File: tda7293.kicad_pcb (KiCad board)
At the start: 2 copper layers, 100 x 48 mm, 70 parts, among them J1 Screw_Terminal_01x04, J2 Screw_Terminal_01x04, J3 Screw_Terminal_01x02, J4 Screw_Terminal_01x03, Q1 BSS84, Q2 2N7002, U1 TDA7293, U2 TDA7293, U3 PC817, U4 MCP1792

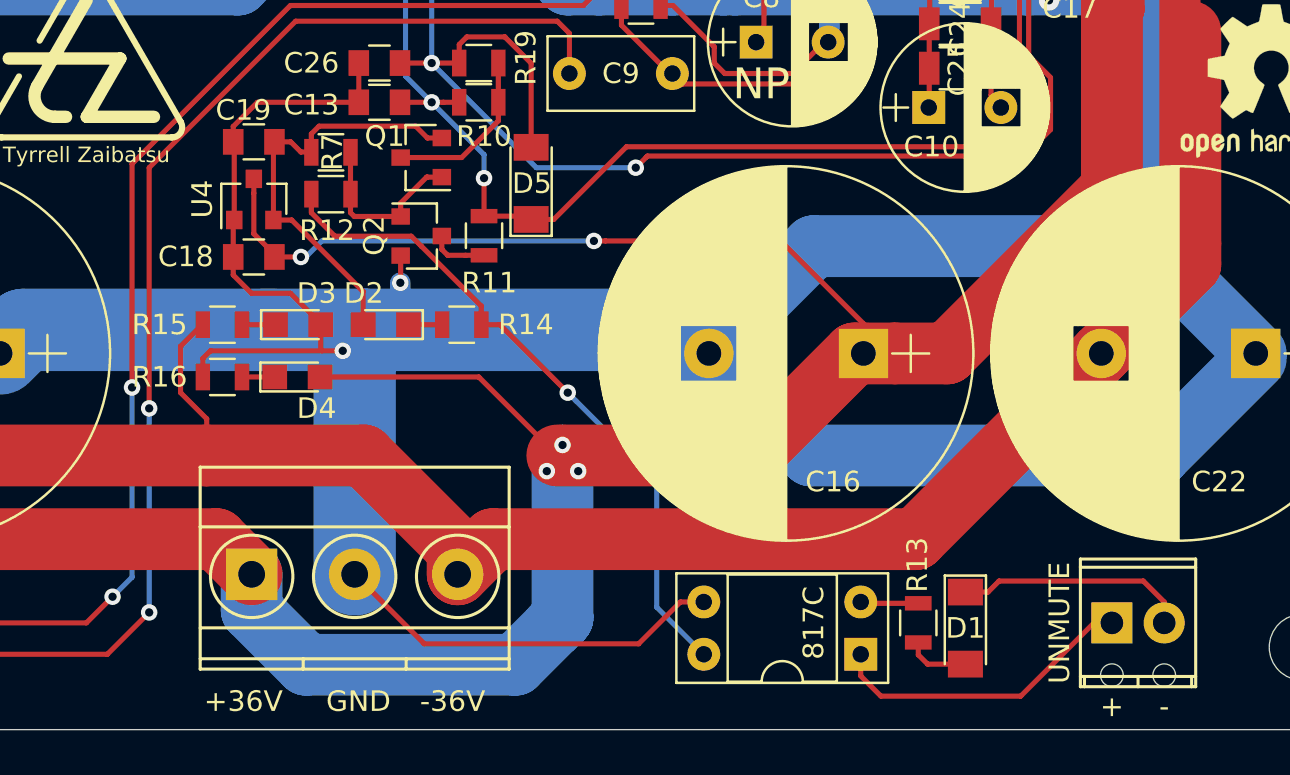
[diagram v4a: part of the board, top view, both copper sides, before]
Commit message: moved a resistor, plotted ready for manufacture
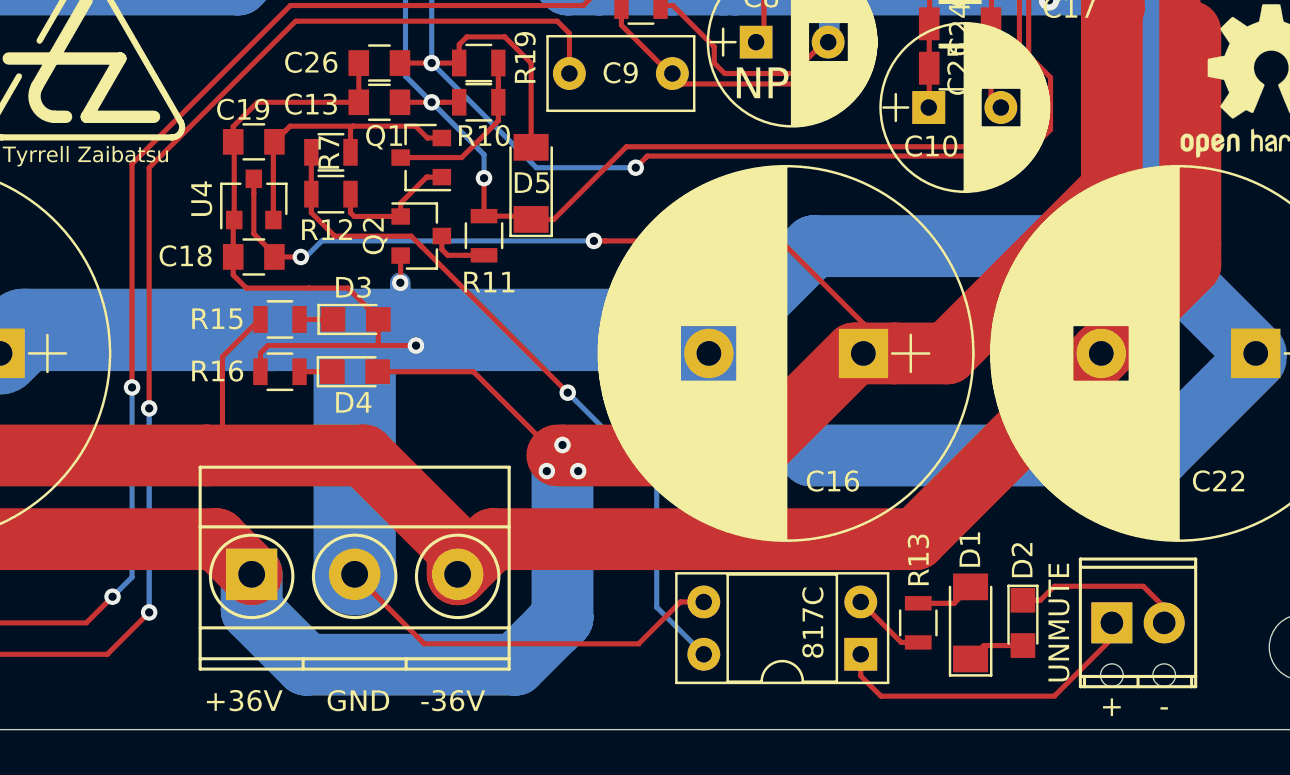
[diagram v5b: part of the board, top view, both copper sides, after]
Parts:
- removed R14: 1k, Resistors_SMD:R_0805
- moved D2 34.2 mm to (107.4, 67.8), turned to 270 degrees
- moved D3 2.81 mm to (75.0, 53.1)
- moved D4 2.81 mm to (75.0, 55.6)
- moved R15 2.81 mm to (71.4, 53.1)
- moved R16 2.81 mm to (71.4, 55.6)
- moved D1 0.36 mm to (104.9, 67.8), turned to 90 degrees
- turned R13 to 270 degrees
- turned R7 to 0 degrees
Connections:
- D2 pad 2: /5V -> Net-(D1-Pad1)
- J3 pad 2: Net-(D1-Pad1) -> Net-(D2-Pad1)
- R7 pad 1: Net-(Q1-Pad1) -> Net-(R12-Pad1)
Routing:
- net Net-(D1-Pad1): track 11.7 -> 2.81 mm
- net /5V: track 20.9 -> 13.9 mm
- net Net-(D2-Pad1): track 1.45 -> 8.32 mm
- net /GND: track 511.8 -> 515.3 mm
- net /VCC: track 212.3 -> 209.6 mm
- net Net-(Q1-Pad1): track 8.61 -> 6.58 mm
- net Net-(R12-Pad1): track 33.4 -> 34.5 mm
- net Net-(R13-Pad2): track 2.82 -> 3.70 mm

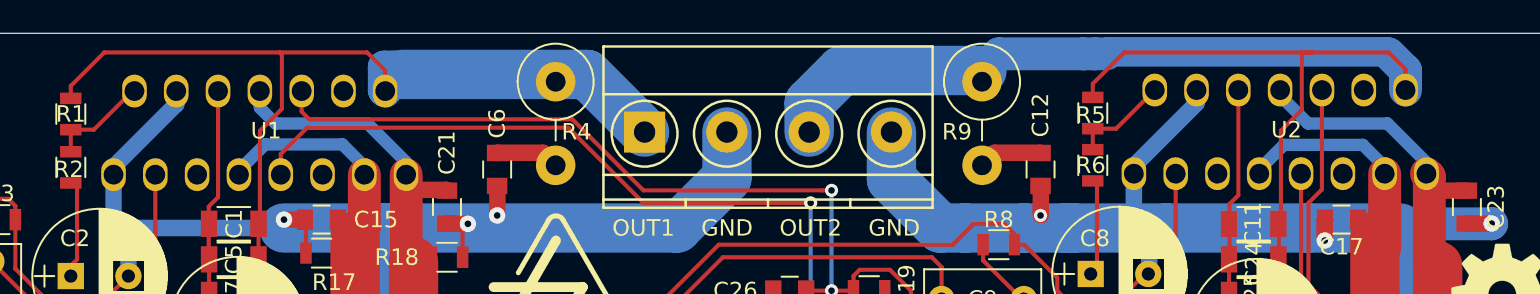
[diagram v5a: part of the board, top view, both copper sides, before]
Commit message: fixed footprint - matching hole size
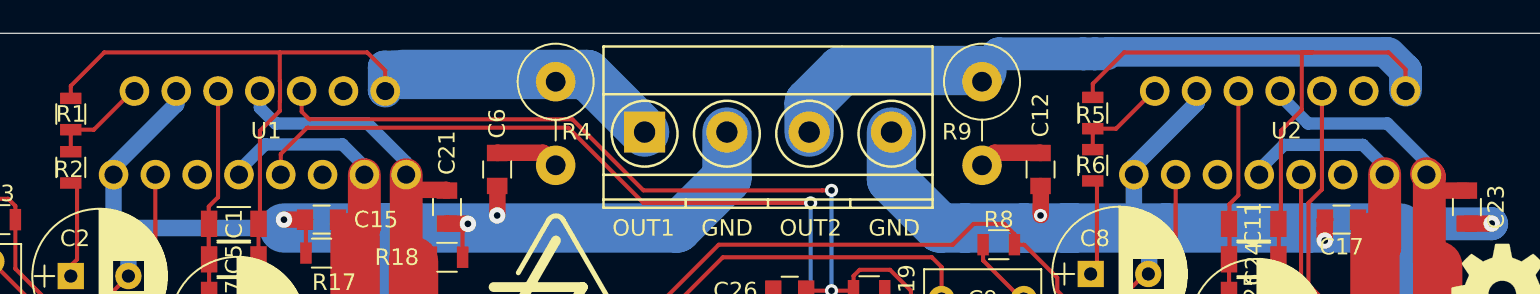
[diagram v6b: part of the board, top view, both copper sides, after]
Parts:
- moved U2 0.06 mm to (106.0, 28.5)
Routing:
- net Net-(C3-Pad1): track 22.8 -> 22.3 mm

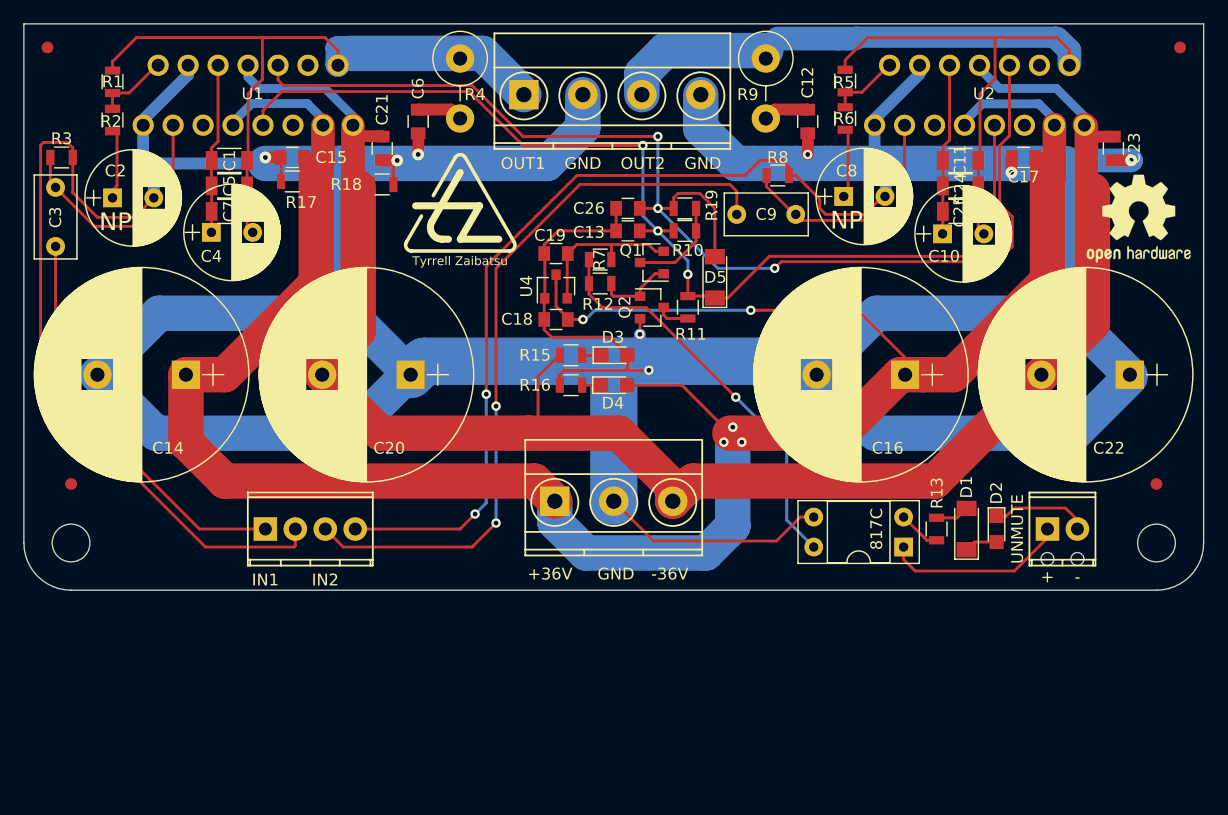
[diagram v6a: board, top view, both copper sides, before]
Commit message: Redrafted as Rev.B: hum-break resistors, better GND topology, fuses, room for heatsink screwdrivers!
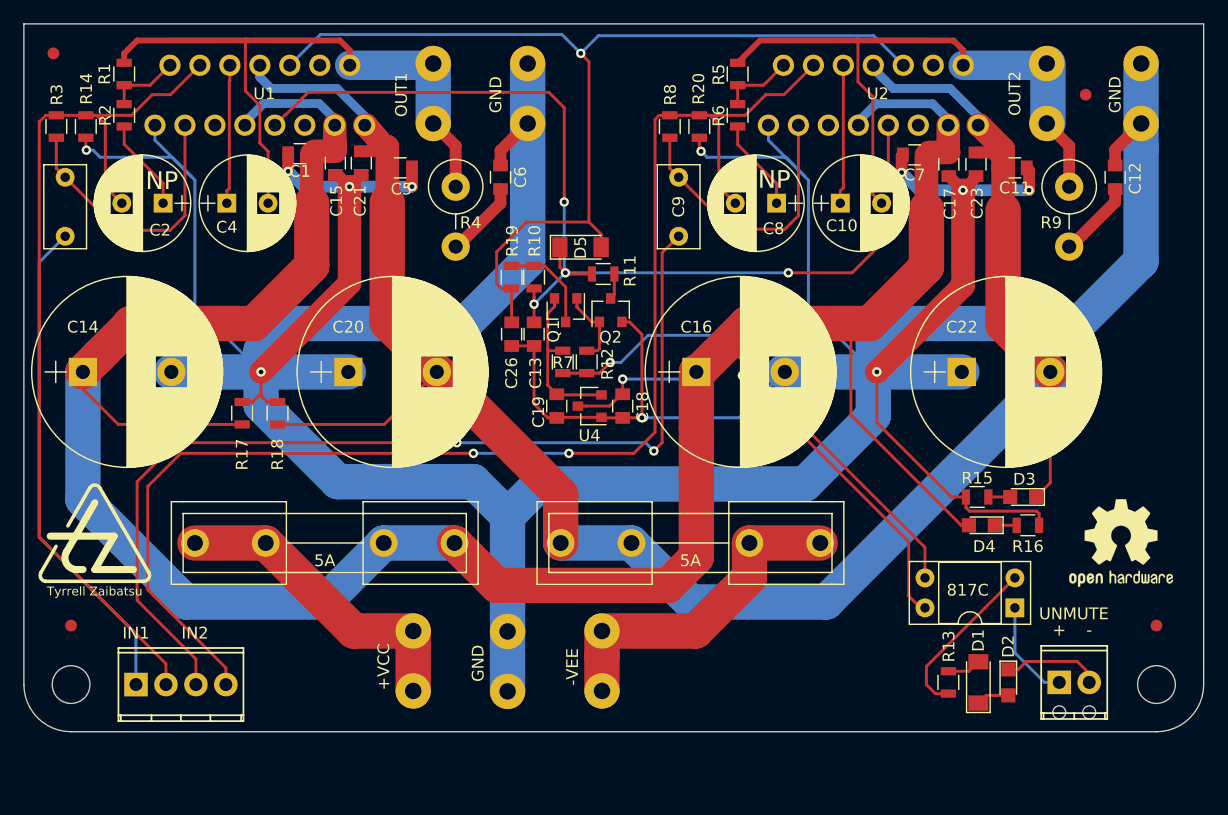
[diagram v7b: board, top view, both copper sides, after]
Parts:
- removed C24, C25: 10u, Capacitors_SMD:C_1206
- added F1: 4A, power:Fuseholder5x20_6mm, F.Cu at (60.5, 69.0)
- added F2: 4A, power:Fuseholder5x20_6mm, F.Cu at (71.5, 69.0)
- added J5: Conn_01x01_Male, power:FASTON250P_5.08mm_male_vertical, F.Cu at (111.7, 30.9)
- added J6: Conn_01x01_Male, power:FASTON250P_5.08mm_male_vertical, F.Cu at (119.7, 30.9)
- added J7: Conn_01x01_Male, power:FASTON250P_5.08mm_male_vertical, F.Cu at (58.0, 79.0)
- added J8: Conn_01x01_Male, power:FASTON250P_5.08mm_male_vertical, F.Cu at (66.0, 79.0)
- added J9: Conn_01x01_Male, power:FASTON250P_5.08mm_male_vertical, F.Cu at (74.0, 79.0)
- added R14: 15, Resistors_SMD:R_0805, F.Cu at (30.2, 33.7)
- added R20: 15, Resistors_SMD:R_0805, F.Cu at (82.2, 33.7)
- C1, C11, C5, C7: value 10u -> 1u; footprint Capacitors_SMD:C_1206 -> Capacitors_SMD:C_0805
- C14, C16, C20, C22: value 3300u -> 1000u; footprint Capacitors_ThroughHole:CP_Radial_D18.0mm_P7.50mm -> Capacitors_ThroughHole:CP_Radial_D16.0mm_P7.50mm
- J2: value Screw_Terminal_01x04 -> Conn_01x01_Male; footprint Terminals_Phoenix:TerminalBlock_Phoenix_MKDS1.5-4pol -> power:FASTON250P_5.08mm_male_vertical
- J4: value Screw_Terminal_01x03 -> Conn_01x01_Male; footprint Terminals_Phoenix:TerminalBlock_Phoenix_MKDS1.5-3pol -> power:FASTON250P_5.08mm_male_vertical
- moved FID3 95.5 mm to (27.5, 27.5)
- moved FID2 88.1 mm to (115.0, 31.0)
- moved C7 58.3 mm to (100.5, 36.1)
- moved REF** 41.8 mm to (31.0, 69.0)
- moved R16 40.5 mm to (110.1, 67.5), turned to 0 degrees
- moved D3 36.7 mm to (109.7, 65.1), turned to 180 degrees
- moved R15 36.5 mm to (105.8, 65.1), turned to 0 degrees
- moved J4 34.6 mm to (67.7, 30.9)
- moved D4 33.4 mm to (106.2, 67.5), turned to 180 degrees
- moved R9 27.9 mm to (113.6, 38.8)
- moved REF*** 27.5 mm to (118.0, 69.0)
- moved C12 26.5 mm to (117.5, 38.0), turned to 90 degrees
- moved R18 21.3 mm to (46.5, 58.0), turned to 90 degrees
- moved R17 20.1 mm to (43.5, 58.0), turned to 270 degrees
- moved C16 17.7 mm to (82.0, 54.5), turned to 0 degrees
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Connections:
- C1 pad 1: /OUT1 -> /VCC
- C1 pad 2: Net-(C1-Pad2) -> /GND
- C11 pad 1: /OUT2 -> /GND
- C11 pad 2: Net-(C10-Pad1) -> /VEE
- C2 pad 2: /GND -> Net-(C2-Pad2)
- C4 pad 1: Net-(C1-Pad2) -> Net-(C4-Pad1)
- C5 pad 1: /OUT1 -> /GND
- C5 pad 2: Net-(C1-Pad2) -> /VEE
- C7 pad 1: /OUT1 -> /VCC
- C7 pad 2: Net-(C1-Pad2) -> /GND
- C8 pad 2: /GND -> Net-(C8-Pad2)
- D3 pad 1: Net-(D3-Pad1) -> /VEE
- D3 pad 2: /GND -> Net-(D3-Pad2)
- J1 pad 2: /GND -> Net-(C2-Pad2)
- J1 pad 4: /GND -> Net-(C8-Pad2)
- J4 pad 1: /VCC -> /GND
- R15 pad 1: Net-(D3-Pad1) -> /GND
- R15 pad 2: /VEE -> Net-(D3-Pad2)
- R3 pad 1: /GND -> Net-(C2-Pad2)
- R8 pad 1: /GND -> Net-(C8-Pad2)
- U1 pad 4: /GND -> Net-(C2-Pad2)
- U1 pad 6: Net-(C1-Pad2) -> Net-(C4-Pad1)
- U2 pad 4: /GND -> Net-(C8-Pad2)
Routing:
- net Net-(C8-Pad2): track 0.00 -> 115.5 mm, vias 0 -> 2
- net Net-(C2-Pad2): track 0.00 -> 77.0 mm
- net /GND: track 515.3 -> 442.9 mm, vias 10 -> 11
- net Net-(F2-Pad2): track 0.00 -> 28.4 mm
- net /OUT2: track 81.4 -> 54.6 mm
- net Net-(F1-Pad2): track 0.00 -> 26.7 mm
- net Net-(C9-Pad2): track 63.1 -> 83.8 mm
- net /VCC: track 209.6 -> 229.9 mm, vias 5 -> 1
- net /VEE: track 153.4 -> 173.3 mm
- net Net-(C1-Pad2): track 14.4 -> 0.00 mm
- net /MUTE: track 103.1 -> 89.1 mm, vias 3 -> 1
- net Net-(C4-Pad1): track 0.00 -> 11.8 mm
- net Net-(R13-Pad2): track 3.70 -> 14.3 mm
- net Net-(R12-Pad1): track 34.5 -> 45.1 mm, vias 1 -> 2
- net Net-(C3-Pad2): track 34.6 -> 42.3 mm
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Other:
- board size 100 x 48 mm -> 100 x 60 mm
- board text added: "+VCC"
- board text added: "-VEE"
- board text added: "5A"
- board text added: "Stereo TDA7293/TDA7294 Rev.B 202201 william@brodie-tyrrell.org github.com/phenidone"
- board text removed: "+36V"
- board text removed: "-36V"
- board text removed: "Stereo TDA7293/TDA7294 Rev.A 202111 william@brodie-tyrrell.org github.com/phenidone"

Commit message: silk-screen updates, turd-polishing, plotted gerbers
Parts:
- removed C21, C23: 1u, Capacitors_SMD:C_0805
- removed C22: 1000u, Capacitors_ThroughHole:CP_Radial_D16.0mm_P7.50mm
- removed C26: 10u, Capacitors_SMD:C_0805
- removed D4: LED, LEDs:LED_0805
- removed D5: LL4148, Diodes_SMD:D_MiniMELF
- removed the REF*** at (106.0, 62.0)
- added H3: MountingHole, Mounting_Holes:MountingHole_3.2mm_M3, F.Cu at (47.0, 41.0)
- added H4: MountingHole, Mounting_Holes:MountingHole_3.2mm_M3, F.Cu at (97.0, 41.0)
- added J10: Conn_01x01_Male, power:FASTON250P_5.08mm_male_vertical, F.Cu at (48.0, 83.3)
- added J11: Conn_01x01_Male, power:FASTON250P_5.08mm_male_vertical, F.Cu at (102.0, 83.3)
- added J12: Conn_01x01_Male, power:FASTON250P_5.08mm_male_vertical, F.Cu at (83.0, 83.3)
- added R21: 27k, Resistors_SMD:R_0805, F.Cu at (101.5, 63.0)
- added R22: 27k, Resistors_SMD:R_0805, F.Cu at (106.5, 63.0)
- added R23: 1k, Resistors_SMD:R_0805, F.Cu at (69.0, 65.4)
- C10, C4: value 22u -> 1u; footprint Capacitors_ThroughHole:CP_Radial_D8.0mm_P3.50mm -> Capacitors_ThroughHole:C_Rect_L7.0mm_W3.5mm_P5.00mm
- C11, C5: value 1u -> 22u; footprint Capacitors_SMD:C_0805 -> Capacitors_ThroughHole:CP_Radial_D6.3mm_P2.50mm
- C13, C19: value 10u -> 1000u; footprint Capacitors_SMD:C_0805 -> Capacitors_ThroughHole:CP_Radial_D16.0mm_P7.50mm
- C14, C16, C20: value 1000u -> 1u; footprint Capacitors_ThroughHole:CP_Radial_D16.0mm_P7.50mm -> Capacitors_SMD:C_0805
- C15, C17: value 1u -> 1000u; footprint Capacitors_SMD:C_0805 -> Capacitors_ThroughHole:CP_Radial_D16.0mm_P7.50mm
- C2, C8: value 22u NP -> 10u; footprint Capacitors_ThroughHole:CP_Radial_D8.0mm_P3.50mm -> Capacitors_SMD:C_0805
- C3, C9: value 1u -> 22u NP; footprint Capacitors_ThroughHole:C_Rect_L7.0mm_W3.5mm_P5.00mm -> Capacitors_ThroughHole:CP_Radial_D8.0mm_P3.50mm
- C7: value 1u -> 10u
- D2: value LED -> LL4148; footprint LEDs:LED_0805 -> Diodes_SMD:D_MiniMELF
- J1: value Screw_Terminal_01x04 -> Screw_Terminal_01x02; footprint Terminals_Phoenix:TerminalBlock_Phoenix_MPT-2.54mm_4pol -> Terminals_Phoenix:TerminalBlock_Phoenix_MPT-2.54mm_2pol
- J6: value Conn_01x01_Male -> Screw_Terminal_01x02; footprint power:FASTON250P_5.08mm_male_vertical -> Terminals_Phoenix:TerminalBlock_Phoenix_MPT-2.54mm_2pol
- R10: value 10k -> 27k
- R11: value 1k -> 3k9
- R12: value 100 -> 1k
- R13: value 3k9 -> 22k
- R14: value 15 -> 680
- R15: value 10k -> 22k
- R16: value 10k -> 2R7; footprint Resistors_SMD:R_0805 -> Resistors_ThroughHole:R_Axial_DIN0414_L11.9mm_D4.5mm_P5.08mm_Vertical
- R17: value 27k -> 10
- R18: value 27k -> 0R
- R20: value 15 -> 27k
- R4, R9: value 2R7 -> 10k; footprint Resistors_ThroughHole:R_Axial_DIN0414_L11.9mm_D4.5mm_P5.08mm_Vertical -> Resistors_SMD:R_0805
- R5: value 22k -> 2R7; footprint Resistors_SMD:R_0805 -> Resistors_ThroughHole:R_Axial_DIN0414_L11.9mm_D4.5mm_P5.08mm_Vertical
- R6: value 680 -> 100
- R7: value 10k -> 10
- R8: value 22k -> 0R
- U1: value TDA7293 -> MCP1792; footprint power:Multiwatt15V -> TO_SOT_Packages_SMD:SOT-23
- U4: value MCP1792 -> TDA7293; footprint TO_SOT_Packages_SMD:SOT-23 -> power:Multiwatt15V
- moved FID1 106.0 mm to (27.0, 27.0)
- moved FID4 94.1 mm to (123.0, 81.0)
- moved J5 89.6 mm to (39.0, 83.3)
- moved J8 72.3 mm to (120.0, 31.0), turned to 0 degrees
- moved J7 71.5 mm to (111.0, 31.0)
- moved R13 56.0 mm to (84.2, 28.2), turned to 90 degrees
- moved C20 55.3 mm to (105.0, 37.2), turned to 90 degrees
- moved R14 54.0 mm to (84.2, 31.8)
- moved FID3 53.5 mm to (27.0, 81.0)
- moved U2 51.0 mm to (46.0, 28.5)
- moved C15 49.4 mm to (96.0, 58.0), turned to 180 degrees
- moved C19 49.3 mm to (119.5, 58.0), turned to 180 degrees
- moved D1 49.3 mm to (72.0, 45.0), turned to 270 degrees
- moved R11 49.1 mm to (117.8, 68.7), turned to 90 degrees
- moved C17 46.9 mm to (61.5, 58.0), turned to 180 degrees
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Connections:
- C1 pad 1: /VCC -> Net-(C1-Pad1)
- C1 pad 2: /GND -> /SGND
- C10 pad 2: /OUT2 -> Net-(C10-Pad2)
- C11 pad 1: /GND -> Net-(C11-Pad1)
- C11 pad 2: /VEE -> /OUTR
- C12 pad 2: /GND -> /RGND
- C13 pad 1: /GND -> /VCC
- C13 pad 2: /STBY -> /LGND
- C14 pad 2: /GND -> /LGND
- C15 pad 2: /GND -> /RGND
- C16 pad 2: /GND -> /RGND
- C17 pad 1: /VCC -> /LGND
- C17 pad 2: /GND -> /VEE
- C18 pad 1: /VCC -> /LGND
- C18 pad 2: /GND -> /VEE
- C19 pad 1: /5V -> /RGND
- C19 pad 2: /GND -> /VEE
- C2 pad 1: Net-(C2-Pad1) -> /5V
- C2 pad 2: Net-(C2-Pad2) -> /SGND
- C20 pad 1: /GND -> /RGND
- C4 pad 2: /OUT1 -> Net-(C4-Pad2)
- C5 pad 1: /GND -> Net-(C5-Pad1)
- C5 pad 2: /VEE -> /OUTL
- C6 pad 2: /GND -> /LGND
- C7 pad 1: /VCC -> /SGND
- C7 pad 2: /GND -> /STBY
- C8 pad 1: Net-(C8-Pad1) -> /SGND
- C8 pad 2: Net-(C8-Pad2) -> /MUTE
- D1 pad 1: Net-(D1-Pad1) -> /STBY
- D1 pad 2: Net-(D1-Pad2) -> /MUTE
- D2 pad 2: Net-(D1-Pad1) -> Net-(D2-Pad2)
- D3 pad 1: /VEE -> Net-(D3-Pad1)
- D3 pad 2: Net-(D3-Pad2) -> Net-(D2-Pad1)
- J1 pad 2: Net-(C2-Pad2) -> Net-(C4-Pad2)
- J2 pad 1: /OUT1 -> /OUTL
- J3 pad 2: Net-(D2-Pad1) -> Net-(D3-Pad1)
- J4 pad 1: /GND -> /LGND
- J5 pad 1: /OUT2 -> /SGND
- J6 pad 1: /GND -> Net-(C9-Pad2)
- J7 pad 1: Net-(F1-Pad2) -> /OUTR
- J8 pad 1: /GND -> /RGND
- J9 pad 1: Net-(F2-Pad2) -> Net-(F1-Pad2)
- Q2 pad 2: /GND -> /SGND
- R1 pad 2: /OUT1 -> /OUTL
- R10 pad 2: /STBY -> /MUTE
- R11 pad 1: /STBY -> Net-(D2-Pad2)
- R11 pad 2: Net-(Q2-Pad3) -> Net-(R11-Pad2)
- R12 pad 1: Net-(R12-Pad1) -> /STBY
- R12 pad 2: Net-(Q1-Pad1) -> Net-(Q2-Pad3)
- R13 pad 1: Net-(D1-Pad2) -> Net-(R13-Pad1)
- R13 pad 2: Net-(R13-Pad2) -> /OUTR
- R14 pad 1: Net-(C2-Pad2) -> Net-(R13-Pad1)
- R14 pad 2: /GND -> Net-(C9-Pad1)
- R15 pad 1: /GND -> Net-(C9-Pad2)
- R15 pad 2: Net-(D3-Pad2) -> Net-(C10-Pad1)
- R16 pad 1: Net-(D4-Pad1) -> /OUTR
- R16 pad 2: /GND -> Net-(C12-Pad1)
- R17 pad 1: /GND -> Net-(C9-Pad2)
- R17 pad 2: /VCC -> Net-(R17-Pad2)
- R18 pad 1: /VEE -> Net-(R17-Pad2)
- R18 pad 2: /GND -> /SGND
- R19 pad 1: Net-(Q1-Pad3) -> /LGND
- R19 pad 2: /MUTE -> /VCC
- R2 pad 2: Net-(C2-Pad1) -> Net-(C3-Pad1)
- R20 pad 1: Net-(C8-Pad2) -> /VEE
- R20 pad 2: /GND -> /LGND
- R3 pad 1: Net-(C2-Pad2) -> Net-(C3-Pad2)
- R3 pad 2: Net-(C3-Pad1) -> Net-(C4-Pad1)
- R4 pad 1: /OUT1 -> Net-(R4-Pad1)
- R4 pad 2: Net-(C6-Pad1) -> /5V
- R5 pad 1: Net-(R5-Pad1) -> /OUTL
- R5 pad 2: /OUT2 -> Net-(C6-Pad1)
- R6 pad 1: Net-(R5-Pad1) -> Net-(R4-Pad1)
- R6 pad 2: Net-(C8-Pad1) -> Net-(Q1-Pad1)
- R7 pad 1: Net-(R12-Pad1) -> Net-(C3-Pad2)
- R7 pad 2: /5V -> Net-(R7-Pad2)
- R8 pad 1: Net-(C8-Pad2) -> Net-(R7-Pad2)
- R8 pad 2: Net-(C9-Pad1) -> /SGND
- R9 pad 1: /OUT2 -> Net-(Q1-Pad3)
- R9 pad 2: Net-(C12-Pad1) -> /STBY
- U1 pad 1: /GND -> /SGND
- U1 pad 2: Net-(R1-Pad1) -> /5V
- U1 pad 3: Net-(C3-Pad1) -> Net-(C1-Pad1)
- U2 pad 1: /GND -> /SGND
- U2 pad 14: /OUT2 -> /OUTL
- U2 pad 2: Net-(R5-Pad1) -> Net-(R1-Pad1)
- U2 pad 3: Net-(C9-Pad1) -> Net-(C4-Pad1)
- U2 pad 4: Net-(C8-Pad2) -> Net-(R7-Pad2)
- U2 pad 5: /CLIP2 -> /CLIP1
- U2 pad 6: Net-(C10-Pad1) -> Net-(C5-Pad1)
- U3 pad 2: Net-(R13-Pad2) -> Net-(R11-Pad2)
- U3 pad 3: /GND -> /SGND
- U3 pad 4: Net-(R12-Pad1) -> Net-(R4-Pad1)
- U4 pad 1: /GND -> /SGND
- U4 pad 2: /5V -> Net-(R13-Pad1)
- U4 pad 3: /VCC -> Net-(C10-Pad1)
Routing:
- net /GND: track 442.9 -> 0.00 mm, vias 11 -> 0
- net /SGND: track 0.00 -> 239.0 mm, vias 0 -> 2
- net /LGND: track 0.00 -> 140.7 mm
- net /RGND: track 0.00 -> 127.0 mm
- net Net-(C8-Pad2): track 115.5 -> 0.00 mm, vias 2 -> 0
- net Net-(R4-Pad1): track 0.00 -> 81.3 mm, vias 0 -> 1
- net /OUTR: track 0.00 -> 77.3 mm
- net Net-(C2-Pad2): track 77.0 -> 0.00 mm
- net /OUTL: track 0.00 -> 76.9 mm
- net Net-(C9-Pad2): track 83.8 -> 14.3 mm, vias 2 -> 0
- net /VCC: track 229.9 -> 168.1 mm, vias 1 -> 0
- net /OUT1: track 55.0 -> 0.00 mm
- net /OUT2: track 54.6 -> 0.00 mm
- net Net-(R12-Pad1): track 45.1 -> 0.00 mm, vias 2 -> 0
- net Net-(C3-Pad2): track 42.3 -> 14.5 mm
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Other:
- board size 100 x 60 mm -> 100 x 65 mm
- board text added: "817"
- board text added: "INL"
- board text added: "INR"
- board text added: "LGND"
- board text added: "OUTL"
- board text added: "OUTR"
- board text added: "RETL"
- board text added: "RETR"
- board text added: "RGND"
- board text added: "SGND"
- board text added: "Stereo TDA7293"
- board text added: "Stereo TDA7293/TDA7294 Rev.B 202204 william@brodie-tyrrell.org github.com/phenidone"
- board text added: "VCC"
- board text added: "VEE"
- board text removed: "+VCC"
- board text removed: "-VEE"
- board text removed: "5A"
- board text removed: "817C"
- board text removed: "IN1"
- board text removed: "IN2"
- board text removed: "OUT1"
- board text removed: "OUT2"
- board text removed: "Stereo TDA7293/TDA7294 Rev.B 202201 william@brodie-tyrrell.org github.com/phenidone"
